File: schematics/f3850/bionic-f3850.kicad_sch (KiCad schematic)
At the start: 11 parts, among them J1 Bionic-P135, J2 Bionic-P245, U1 F3850, U2 11AA010-I/TT, U3 LM78L12

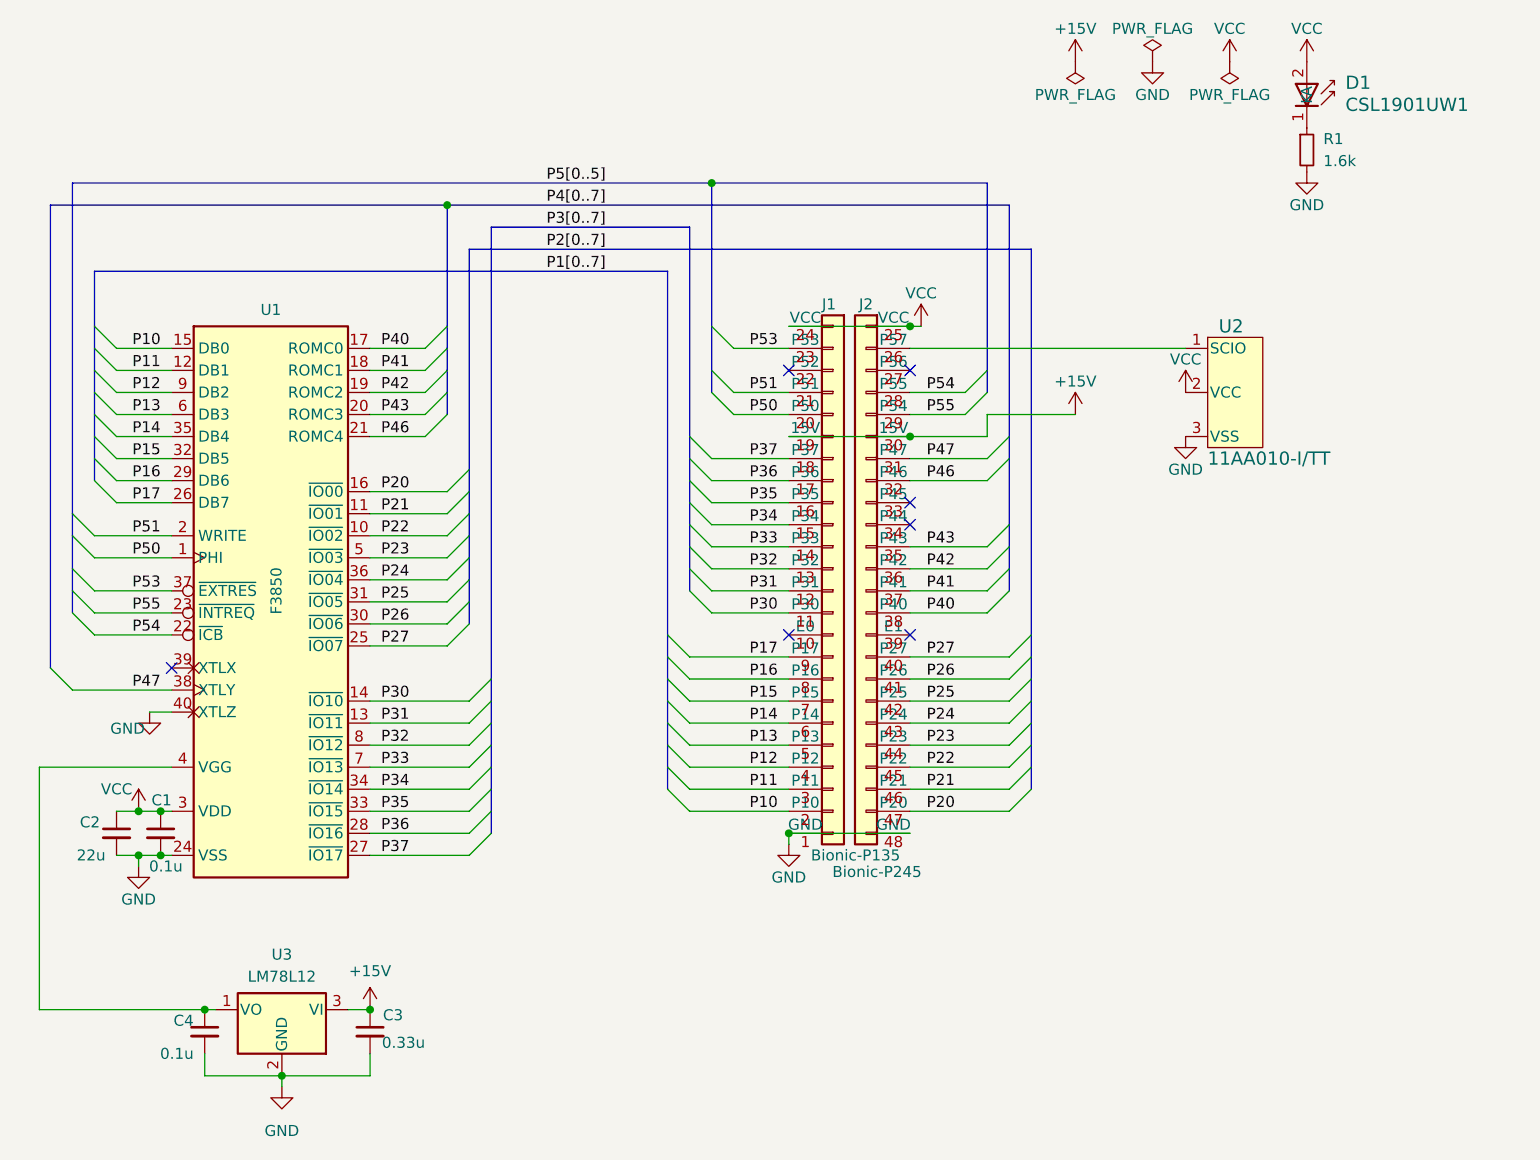
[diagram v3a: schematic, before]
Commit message: [F3850] Fix #INTREQ/#ICB connections
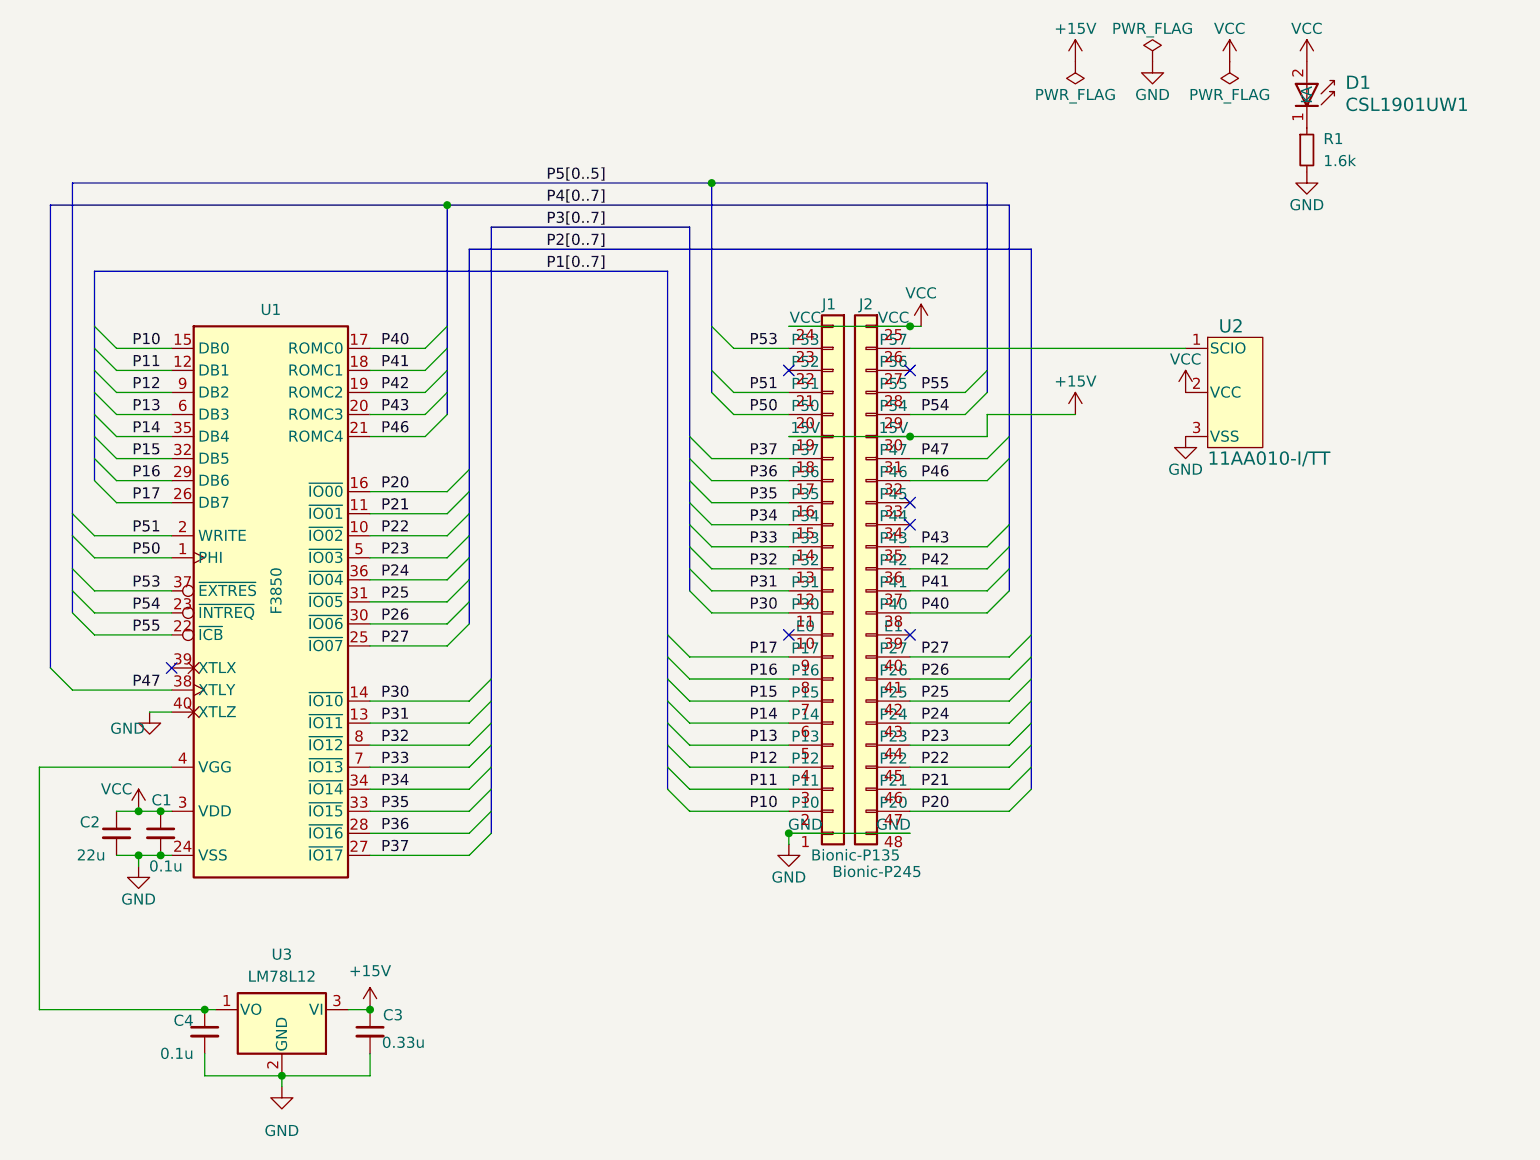
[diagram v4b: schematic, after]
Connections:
- net P54: now also J2.29 (P54), U1.23 (~{INTREQ}); no longer J2.28 (P55), U1.22 (~{ICB})
- net P55: now also J2.28 (P55), U1.22 (~{ICB}); no longer J2.29 (P54), U1.23 (~{INTREQ})
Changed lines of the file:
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@@
 	(title_block
 		(title "BionicF3850")
-		(date "2024-11-01")
+		(date "2024-12-11")
 		(rev "6")
 		(company "Tadashi G. Takaoka")
@@
 	)
 	(label "P26"
-		(at 167.005 104.14 0)
+		(at 166.37 104.14 0)
 		(fields_autoplaced yes)
 		(effects
@@
 	)
 	(label "P41"
-		(at 167.005 93.98 0)
-		(fields_autoplaced yes)
-		(effects
-			(font
-				(size 1.27 1.27)
-			)
-			(justify left bottom)
-		)
-	)
-	(label "P55"
-		(at 167.005 73.66 0)
+		(at 166.37 93.98 0)
 		(fields_autoplaced yes)
 		(effects
@@
 		)
 	)
+	(label "P54"
+		(at 166.37 73.66 0)
+		(fields_autoplaced yes)
+		(effects
+			(font
+				(size 1.27 1.27)
+			)
+			(justify left bottom)
+		)
+	)
 	(label "P35"
 		(at 149.86 83.82 180)
@@
 	)
 	(label "P27"
-		(at 167.005 101.6 0)
+		(at 166.37 101.6 0)
 		(fields_autoplaced yes)
 		(effects
@@
 	)
 	(label "P21"
-		(at 167.005 116.84 0)
+		(at 166.37 116.84 0)
 		(fields_autoplaced yes)
 		(effects
@@
 	)
 	(label "P25"
-		(at 167.005 106.68 0)
+		(at 166.37 106.68 0)
 		(fields_autoplaced yes)
 		(effects
@@
 	)
 	(label "P40"
-		(at 167.005 96.52 0)
+		(at 166.37 96.52 0)
 		(fields_autoplaced yes)
 		(effects
@@
 	)
 	(label "P22"
-		(at 167.005 114.3 0)
+		(at 166.37 114.3 0)
 		(fields_autoplaced yes)
 		(effects
@@
 	)
 	(label "P46"
-		(at 167.005 81.28 0)
+		(at 166.37 81.28 0)
 		(fields_autoplaced yes)
 		(effects
@@
 	)
 	(label "P24"
-		(at 167.005 109.22 0)
-		(fields_autoplaced yes)
-		(effects
-			(font
-				(size 1.27 1.27)
-			)
-			(justify left bottom)
-		)
-	)
-	(label "P55"
+		(at 166.37 109.22 0)
+		(fields_autoplaced yes)
+		(effects
+			(font
+				(size 1.27 1.27)
+			)
+			(justify left bottom)
+		)
+	)
+	(label "P54"
 		(at 78.74 96.52 180)
 		(fields_autoplaced yes)
@@
 	)
 	(label "P43"
-		(at 167.005 88.9 0)
+		(at 166.37 88.9 0)
 		(fields_autoplaced yes)
 		(effects
@@
 		)
 	)
-	(label "P54"
+	(label "P55"
 		(at 78.74 99.06 180)
 		(fields_autoplaced yes)
@@
 		)
 	)
-	(label "P54"
-		(at 167.005 71.12 0)
-		(fields_autoplaced yes)
-		(effects
-			(font
-				(size 1.27 1.27)
-			)
-			(justify left bottom)
-		)
-	)
 	(label "P14"
 		(at 78.74 76.2 180)
@@
 	)
 	(label "P20"
-		(at 167.005 119.38 0)
+		(at 166.37 119.38 0)
 		(fields_autoplaced yes)
 		(effects
@@
 	)
 	(label "P47"
-		(at 167.005 78.74 0)
+		(at 166.37 78.74 0)
 		(fields_autoplaced yes)
 		(effects
@@
 	)
 	(label "P42"
-		(at 167.005 91.44 0)
+		(at 166.37 91.44 0)
 		(fields_autoplaced yes)
 		(effects
@@
 	)
 	(label "P23"
-		(at 167.005 111.76 0)
-		(fields_autoplaced yes)
-		(effects
+		(at 166.37 111.76 0)
+		(fields_autoplaced yes)
+		(effects
+			(font
+				(size 1.27 1.27)
+			)
+			(justify left bottom)
+		)
+	)
+	(label "P55"
+		(at 166.37 71.12 0)
+		(fields_autoplaced yes)
+		(effects

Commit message: [F3850] Use DCDC converter for +12V
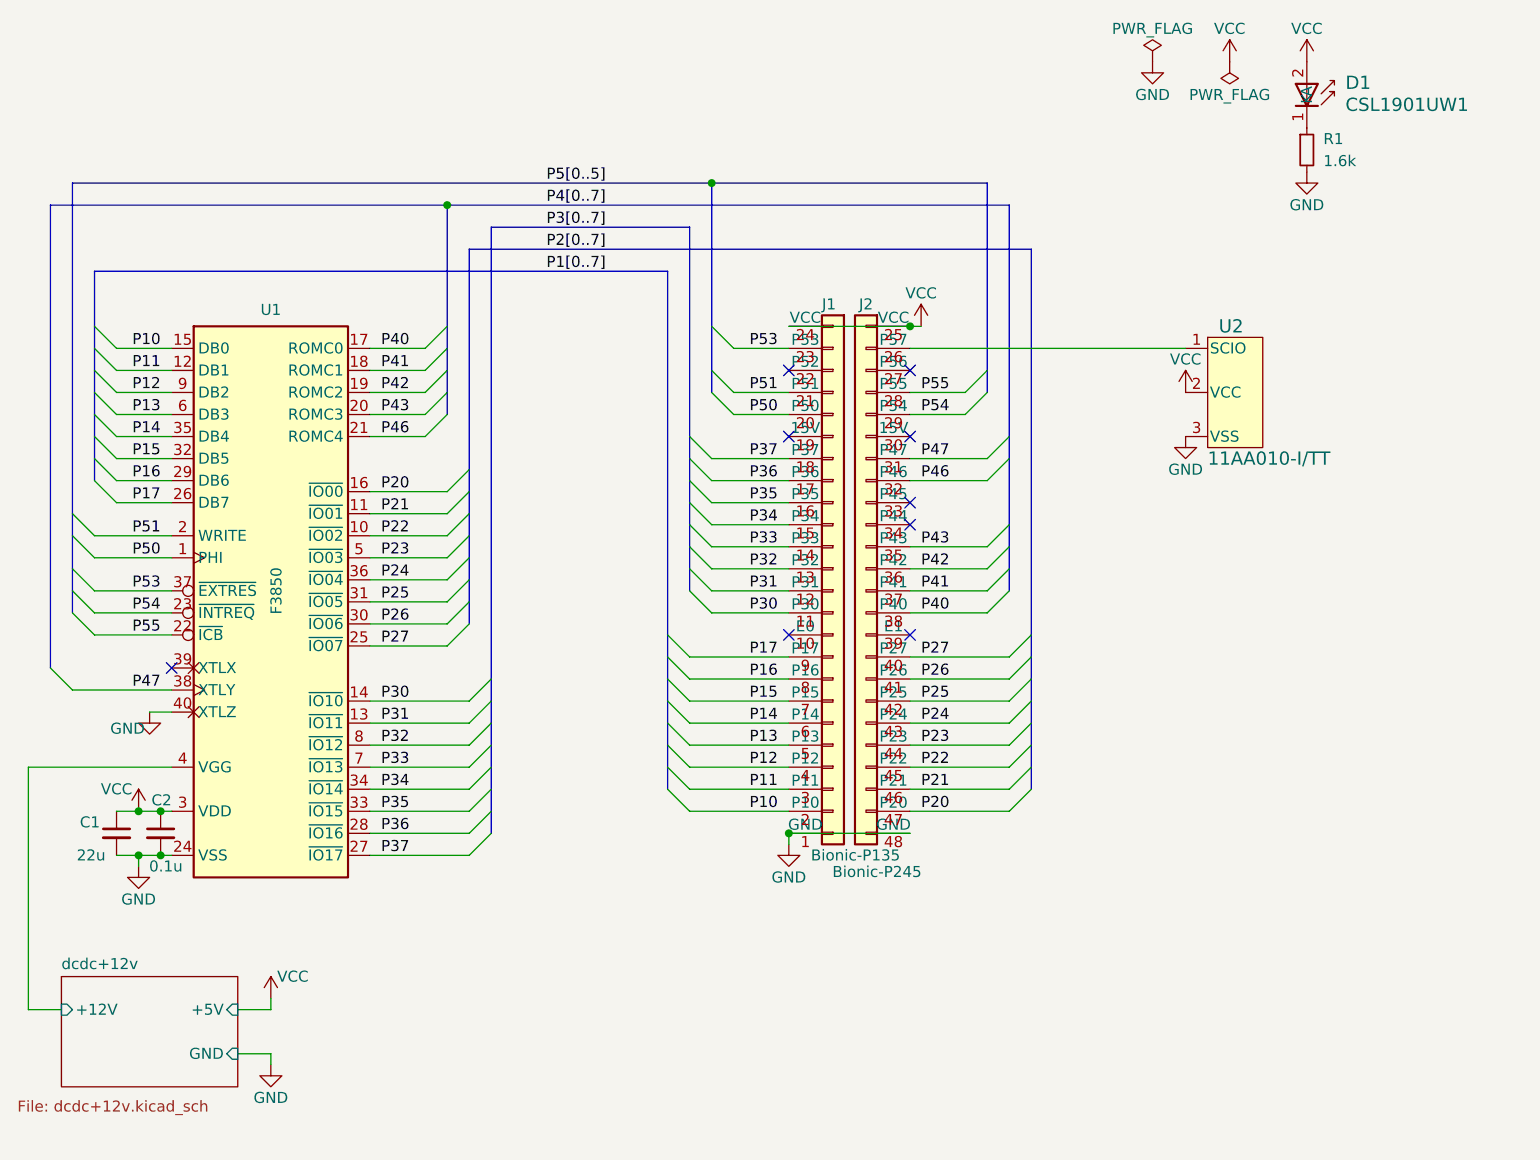
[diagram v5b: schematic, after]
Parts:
- removed C3: 0.33u, Capacitor_SMD:C_1206_3216Metric_Pad1.33x1.80mm_HandSolder, symbol Device:C_Small
- removed C4: 0.1u, Capacitor_SMD:C_0603_1608Metric_Pad1.08x0.95mm_HandSolder, symbol Device:C_Small
- removed U3: LM78L12, 0-LocalLibrary:SOT-89-3_Handsoldering, symbol Regulator_Linear:L78L12_TO92
- renumbered C2 to C1, C1 to C2
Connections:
- net dcdc+12v/+12V: now reaches U1.4 (VGG)
- net +15V: no longer names the net of J1.19 (15V)
- net +15V: no longer J2.30 (15V)
- no-connect marks 7 -> 9
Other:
- added sheet dcdc+12v (dcdc+12v.kicad_sch)
